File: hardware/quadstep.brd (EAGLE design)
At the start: 57.1 x 66 mm, 133 parts, among them U1 A4983, U2 LM317MABDT, U3 A4983, U4 A4983, U5 A4983

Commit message: prototype v020
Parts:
- C5: value 0.1uF -> 0.1uF/100V
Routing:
- net GND: vias 42 -> 58
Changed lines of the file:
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@@
 <text x="45.085" y="54.864" size="1.27" layer="21" font="vector" ratio="18" rot="R270">GND</text>
 <text x="45.085" y="14.859" size="1.27" layer="21" font="vector" ratio="18" rot="R270">GND</text>
+<text x="8.509" y="28.829" size="1.27" layer="22" font="vector" ratio="15" rot="SMR0">GND</text>
+<text x="8.255" y="35.941" size="1.27" layer="22" font="vector" ratio="15" rot="SMR0">VIN</text>
 </plain>
 <attributes>
@@
 <element name="C3" library="SparkFun" package="EIA3216" value="10uF" x="38.1" y="30.48" rot="R90"/>
 <element name="C4" library="SparkFun" package="0805" value="1uF" x="40.64" y="30.48" rot="R270"/>
-<element name="C5" library="SparkFun" package="0402-CAP" value="0.1uF" x="26.67" y="36.83" rot="R90"/>
+<element name="C5" library="SparkFun" package="0402-CAP" value="0.1uF/100V" x="26.67" y="36.83" rot="R90"/>
 <element name="R3" library="SparkFun" package="TRIMPOT-3MM" value="10k" x="7.62" y="60.96" rot="R90"/>
 <element name="C6" library="SparkFun" package="0402-CAP" value="0.1uF" x="11.43" y="40.64" rot="R90"/>
@@
 <wire x1="17.78" y1="41.783" x2="17.78" y2="42.418" width="0.2032" layer="15"/>
 <wire x1="17.78" y1="41.29" x2="17.78" y2="42.418" width="0.2032" layer="1"/>
-<wire x1="22.352" y1="41.402" x2="27.94" y2="46.99" width="0.2032" layer="15"/>
-<wire x1="27.94" y1="46.99" x2="30.607" y2="46.99" width="0.2032" layer="15"/>
-<wire x1="30.607" y1="46.99" x2="32.766" y2="49.149" width="0.2032" layer="15"/>
+<wire x1="22.352" y1="41.402" x2="26.67" y2="45.72" width="0.2032" layer="15"/>
+<wire x1="26.67" y1="45.72" x2="30.099" y2="45.72" width="0.2032" layer="15"/>
+<wire x1="30.099" y1="45.72" x2="31.496" y2="47.117" width="0.2032" layer="15"/>
+<wire x1="31.496" y1="47.117" x2="31.496" y2="47.879" width="0.2032" layer="15"/>
+<wire x1="31.496" y1="47.879" x2="32.766" y2="49.149" width="0.2032" layer="15"/>
 </signal>
 <signal name="EN1">
@@
 <wire x1="6.223" y1="5.08" x2="7.62" y2="6.477" width="0.2032" layer="16"/>
 <via x="9.779" y="19.177" extent="1-16" drill="0.381"/>
-<wire x1="9.779" y1="19.177" x2="9.779" y2="16.129" width="0.2032" layer="2"/>
-<wire x1="9.779" y1="16.129" x2="9.271" y2="15.621" width="0.2032" layer="2"/>
-<wire x1="9.271" y1="15.621" x2="9.271" y2="9.398" width="0.2032" layer="2"/>
+<wire x1="9.271" y1="16.637" x2="9.271" y2="9.398" width="0.2032" layer="2"/>
 <wire x1="9.271" y1="9.398" x2="4.953" y2="5.08" width="0.2032" layer="2"/>
 <wire x1="6.17" y1="5.08" x2="4.953" y2="5.08" width="0.2032" layer="1"/>
 <wire x1="9.779" y1="19.177" x2="11.938" y2="19.177" width="0.2032" layer="15"/>
 <wire x1="11.938" y1="19.177" x2="12.954" y2="20.193" width="0.2032" layer="15"/>
+<wire x1="9.271" y1="16.637" x2="9.017" y2="16.891" width="0.2032" layer="2"/>
+<wire x1="9.017" y1="16.891" x2="9.017" y2="18.415" width="0.2032" layer="2"/>
+<wire x1="9.017" y1="18.415" x2="9.779" y2="19.177" width="0.2032" layer="2"/>
 </signal>
 <signal name="N$23">
@@
 <vertex x="19.7104" y="17.5768"/>
 </polygon>
-<via x="21.5646" y="16.51" extent="1-16" drill="0.381"/>
+<via x="21.5646" y="16.51" extent="1-16" drill="0.508"/>
 <polygon width="0.2032" layer="16" spacing="2.032" isolate="0.2032" orphans="yes" thermals="no">
 <vertex x="21.7932" y="16.9164"/>
@@
 <vertex x="36.2204" y="17.5768"/>
 </polygon>
-<via x="38.0746" y="16.51" extent="1-16" drill="0.381"/>
+<via x="38.0746" y="16.51" extent="1-16" drill="0.508"/>
 <polygon width="0.2032" layer="16" spacing="2.032" isolate="0.2032" orphans="yes" thermals="no">
 <vertex x="37.6428" y="16.9164"/>
@@
 <vertex x="32.3596" y="48.4632"/>
 </polygon>
-<via x="30.5054" y="49.53" extent="1-16" drill="0.381"/>
+<via x="30.5054" y="49.53" extent="1-16" drill="0.508"/>
 <polygon width="0.2032" layer="16" spacing="2.032" isolate="0.2032" orphans="yes" thermals="no">
 <vertex x="30.2768" y="49.1236"/>
@@
 <contactref element="JP2" pad="2"/>
 <contactref element="JP29" pad="4"/>
-<via x="13.9954" y="49.53" extent="1-16" drill="0.381"/>
+<via x="13.9954" y="49.53" extent="1-16" drill="0.508"/>
 <polygon width="0.2032" layer="1" spacing="2.032" isolate="0.2032" orphans="yes" thermals="no">
 <vertex x="15.8496" y="48.5902"/>
@@
 <via x="25.146" y="36.068" extent="1-16" drill="0.381"/>
 <via x="26.162" y="62.103" extent="1-16" drill="0.381"/>
+<via x="13.589" y="47.498" extent="1-16" drill="0.381"/>
+<via x="21.844" y="47.244" extent="1-16" drill="0.381"/>
+<via x="30.099" y="47.498" extent="1-16" drill="0.381"/>
+<via x="40.894" y="47.498" extent="1-16" drill="0.381"/>
+<via x="38.481" y="18.542" extent="1-16" drill="0.381"/>
+<via x="30.099" y="18.669" extent="1-16" drill="0.381"/>
+<via x="22.479" y="18.923" extent="1-16" drill="0.381"/>
+<via x="13.208" y="18.669" extent="1-16" drill="0.381"/>
+<via x="9.652" y="45.974" extent="1-16" drill="0.381"/>
+<via x="9.906" y="17.526" extent="1-16" drill="0.381"/>
+<via x="4.699" y="16.256" extent="1-16" drill="0.381"/>
+<via x="23.368" y="37.592" extent="1-16" drill="0.381"/>
+<via x="25.019" y="40.894" extent="1-16" drill="0.381"/>
+<via x="26.035" y="57.277" extent="1-16" drill="0.381"/>
+<via x="25.908" y="3.683" extent="1-16" drill="0.381"/>
+<via x="27.051" y="29.845" extent="1-16" drill="0.381"/>
 </signal>
 <signal name="N$5">
@@
 <vertex x="15.8496" y="17.5768"/>
 </polygon>
-<via x="13.9954" y="16.51" extent="1-16" drill="0.381"/>
+<via x="13.9954" y="16.51" extent="1-16" drill="0.508"/>
 <polygon width="0.2032" layer="16" spacing="2.032" isolate="0.2032" orphans="yes" thermals="no">
 <vertex x="14.4272" y="16.9164"/>
@@
 <vertex x="32.3596" y="17.5768"/>
 </polygon>
-<via x="30.5054" y="16.51" extent="1-16" drill="0.381"/>
+<via x="30.5054" y="16.51" extent="1-16" drill="0.508"/>
 <polygon width="0.2032" layer="16" spacing="2.032" isolate="0.2032" orphans="yes" thermals="no">
 <vertex x="30.2768" y="16.9164"/>
@@
 <vertex x="36.2204" y="48.4632"/>
 </polygon>
-<via x="38.0746" y="49.53" extent="1-16" drill="0.381"/>
+<via x="38.0746" y="49.53" extent="1-16" drill="0.508"/>
 <polygon width="0.2032" layer="16" spacing="2.032" isolate="0.2032" orphans="yes" thermals="no">
 <vertex x="37.6428" y="49.1236"/>
@@
 <vertex x="19.7104" y="48.4632"/>
 </polygon>
-<via x="21.5646" y="49.53" extent="1-16" drill="0.381"/>
+<via x="21.5646" y="49.53" extent="1-16" drill="0.508"/>
 <polygon width="0.2032" layer="16" spacing="2.032" isolate="0.2032" orphans="yes" thermals="no">
 <vertex x="21.7932" y="49.1236"/>

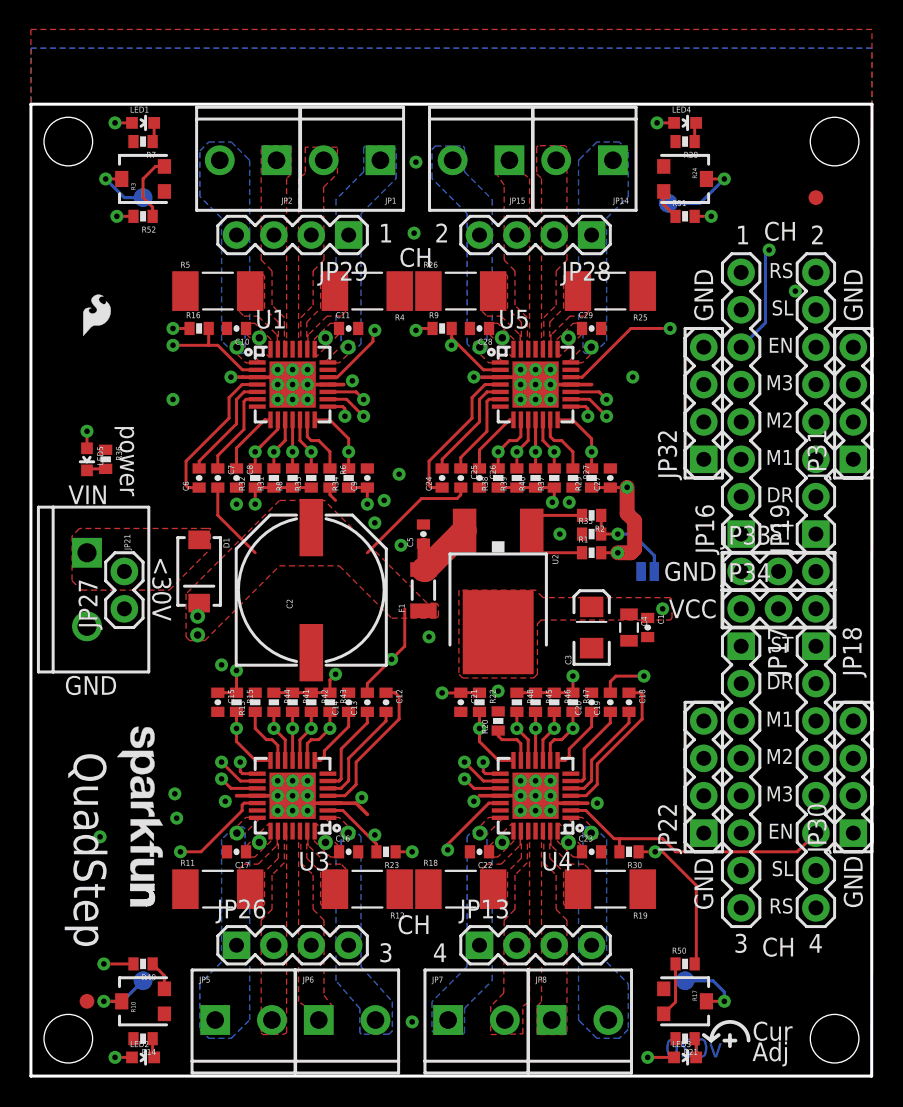
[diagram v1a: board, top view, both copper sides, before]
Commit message: v020 proto
-added standoffs for heatsinks
-changed A4988 FP
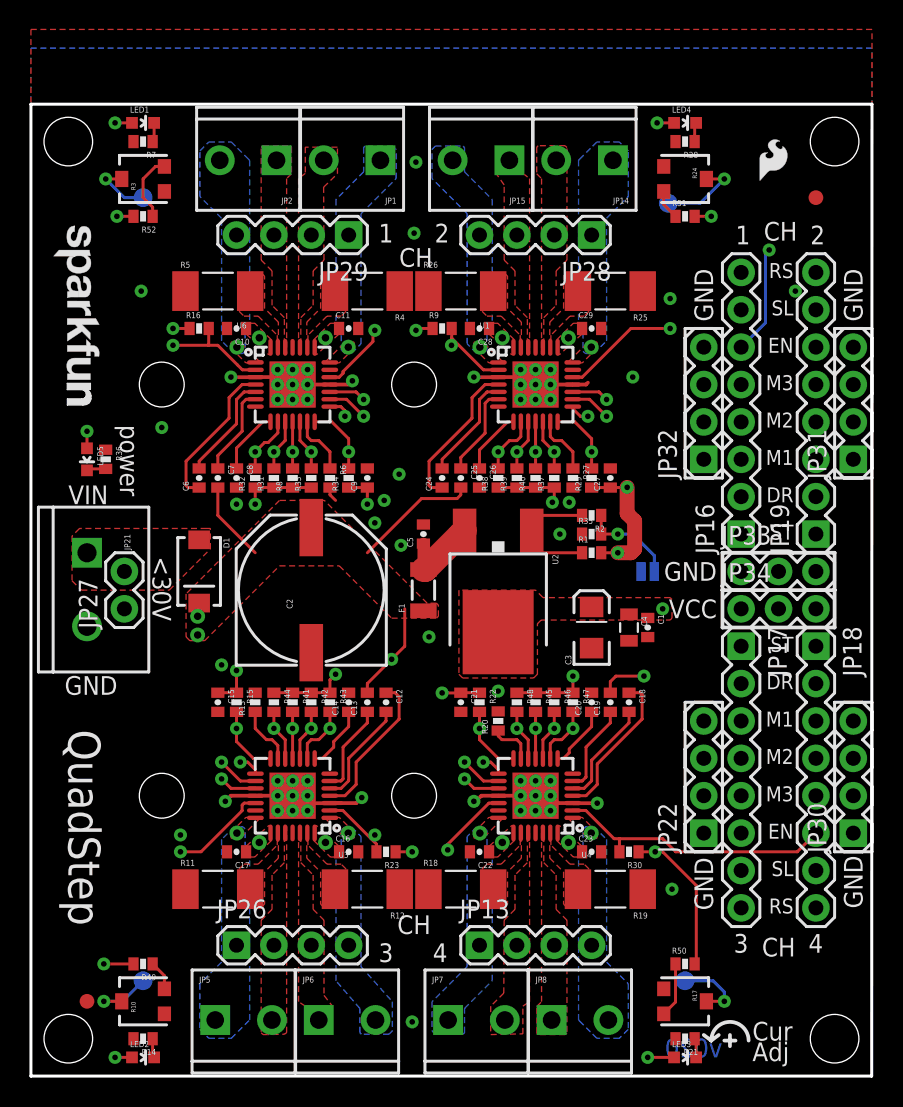
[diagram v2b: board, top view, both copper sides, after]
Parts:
- removed U5: A4983, SparkFun:QFN-28-5MM
- added STANDOFF1, STANDOFF2, STANDOFF3, STANDOFF4: STAND-OFFTIGHT, SparkFun-Electromechanical:STAND-OFF-TIGHT
- added U6: A4988, SparkFun-PowerIC:QFN-28-5MM-1:1
- U1, U3, U4: value A4983 -> A4988; device SparkFun:QFN-28-5MM -> SparkFun-PowerIC:QFN-28-5MM-1:1
- moved JP23 47.2 mm to (49.5, 60.8)
- moved LOGO1 34.3 mm to (1.52, 57.8)
- moved U1 16.5 mm to (34.3, 47.0)
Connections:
- removed net N$45: R25.2, U5.P$23
- new net N$61: R4.2, U6.P$23
- net DIR1: now also U6.P$19; no longer U1.P$19
- net DIR2: now also U1.P$19; no longer U5.P$19
- net EN1: now also U6.P$2; no longer U1.P$2
- net EN2: now also U1.P$2; no longer U5.P$2
- net GND: now also U6.P$18, U6.P$29, U6.P$3; no longer U5.P$18, U5.P$29, U5.P$3
- net MS11: now also U6.P$9; no longer U1.P$9
- net MS12: now also U1.P$9; no longer U5.P$9
- net MS21: now also U6.P$10; no longer U1.P$10
- net MS22: now also U1.P$10; no longer U5.P$10
- net MS31: now also U6.P$11; no longer U1.P$11
- net MS32: now also U1.P$11; no longer U5.P$11
- net N$10: now also U6.P$6; no longer U1.P$6
- net N$11: now also U6.P$8; no longer U1.P$8
- net N$12: now also U6.P$13; no longer U1.P$13
- net N$13: now also U6.P$4; no longer U1.P$4
- net N$14: now also U6.P$17; no longer U1.P$17
- net N$15: now also U6.P$5; no longer U1.P$5
- net N$3: now also U6.P$24; no longer U1.P$24
- net N$41: now also U1.P$21; no longer U5.P$21
- net N$46: now also U1.P$27; no longer U5.P$27
- net N$47: now also U1.P$6; no longer U5.P$6
- net N$48: now also U1.P$8; no longer U5.P$8
- net N$49: now also U1.P$13; no longer U5.P$13
- net N$50: now also U1.P$17; no longer U5.P$17
- net N$51: now also U1.P$4; no longer U5.P$4
- net N$52: now also U1.P$5; no longer U5.P$5
- net N$54: now also U6.P$21; no longer U1.P$21
- net N$55: now also U1.P$24; no longer U5.P$24
- net N$56: now also U1.P$26; no longer U5.P$26
- net N$57: now also U1.P$1; no longer U5.P$1
- net N$6: now also U6.P$26; no longer U1.P$26
- net N$7: now also U6.P$1; no longer U1.P$1
- net N$8: now also R25.2; no longer R4.2
- net N$9: now also U6.P$27; no longer U1.P$27
- net RST1: now also U6.P$12; no longer U1.P$12
- net RST2: now also U1.P$12; no longer U5.P$12
- net SLP1: now also U6.P$14; no longer U1.P$14
- net SLP2: now also U1.P$14; no longer U5.P$14
- net STP1: now also U6.P$16; no longer U1.P$16
- net STP2: now also U1.P$16; no longer U5.P$16
- net VCC: now also U6.P$15; no longer U5.P$15
- net VIN: now also U6.P$22, U6.P$28; no longer U5.P$22, U5.P$28
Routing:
- net RST1: track 41.5 -> 45.7 mm
- net MS23: track 74.6 -> 78.7 mm
- net MS33: track 73.0 -> 76.9 mm
- net SLP3: track 68.9 -> 72.4 mm
- net STP3: track 92.8 -> 96.1 mm
- net SLP1: track 37.3 -> 40.3 mm
- net N$22: track 27.1 -> 25.5 mm
- net MS13: track 108.0 -> 109.5 mm
- net RST3: track 81.2 -> 82.5 mm
- net VCC: track 63.2 -> 61.9 mm
- net N$62: track 0.00 -> 1.02 mm
- net STP4: track 118.8 -> 118.0 mm
- net GND: track 26.4 -> 25.7 mm, vias 58 -> 59
- added copper zone on layer 1, net N$61
- removed copper zone on layer 1, net N$45
